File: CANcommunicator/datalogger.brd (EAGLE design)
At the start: 160 x 100 mm, 50 parts, among them IC1 0.1uF, IC2 1.0uF, IC3 0.1uF, IC4 0.1uF, IC5 LM2937, U1 TXB0104

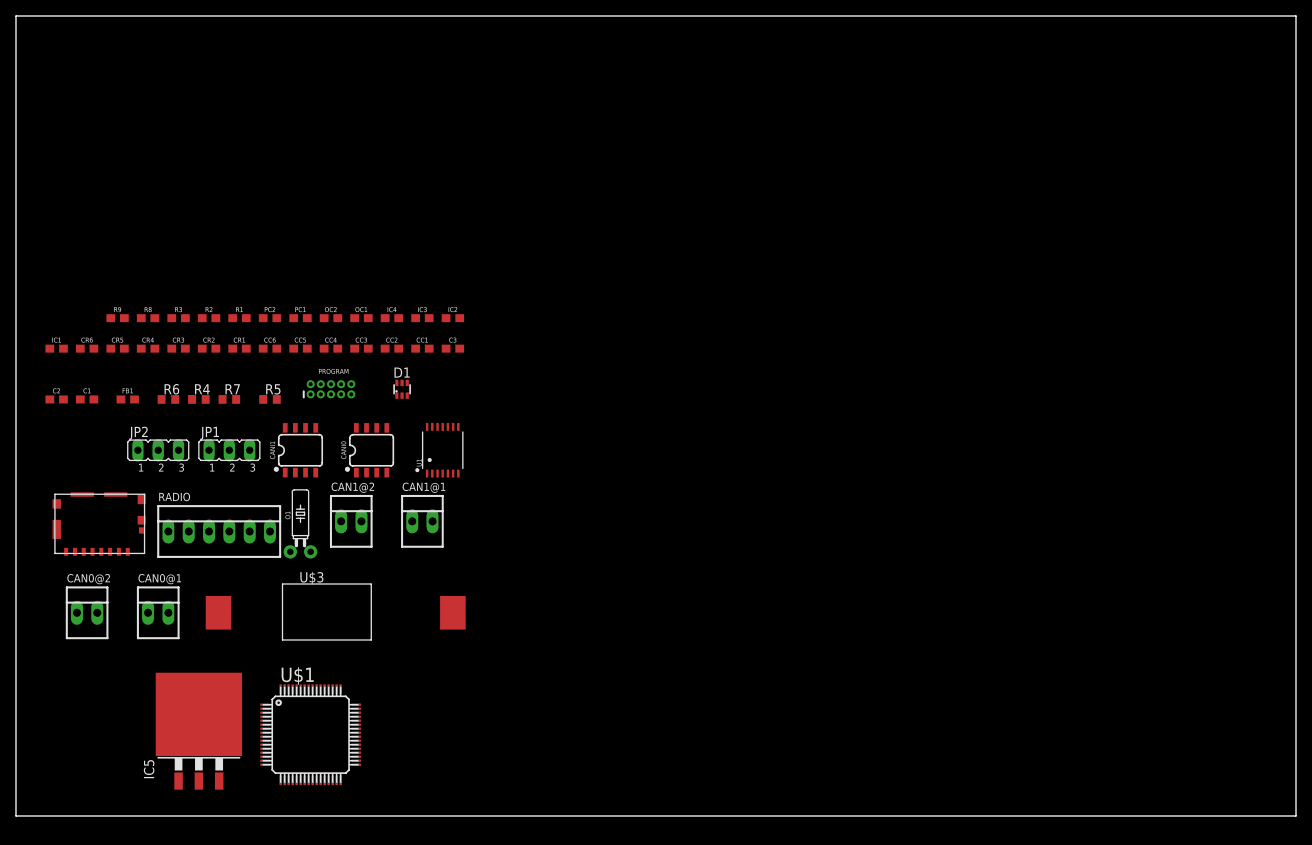
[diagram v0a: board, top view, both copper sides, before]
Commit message: First iteration of CAN datalogger using diode RTC
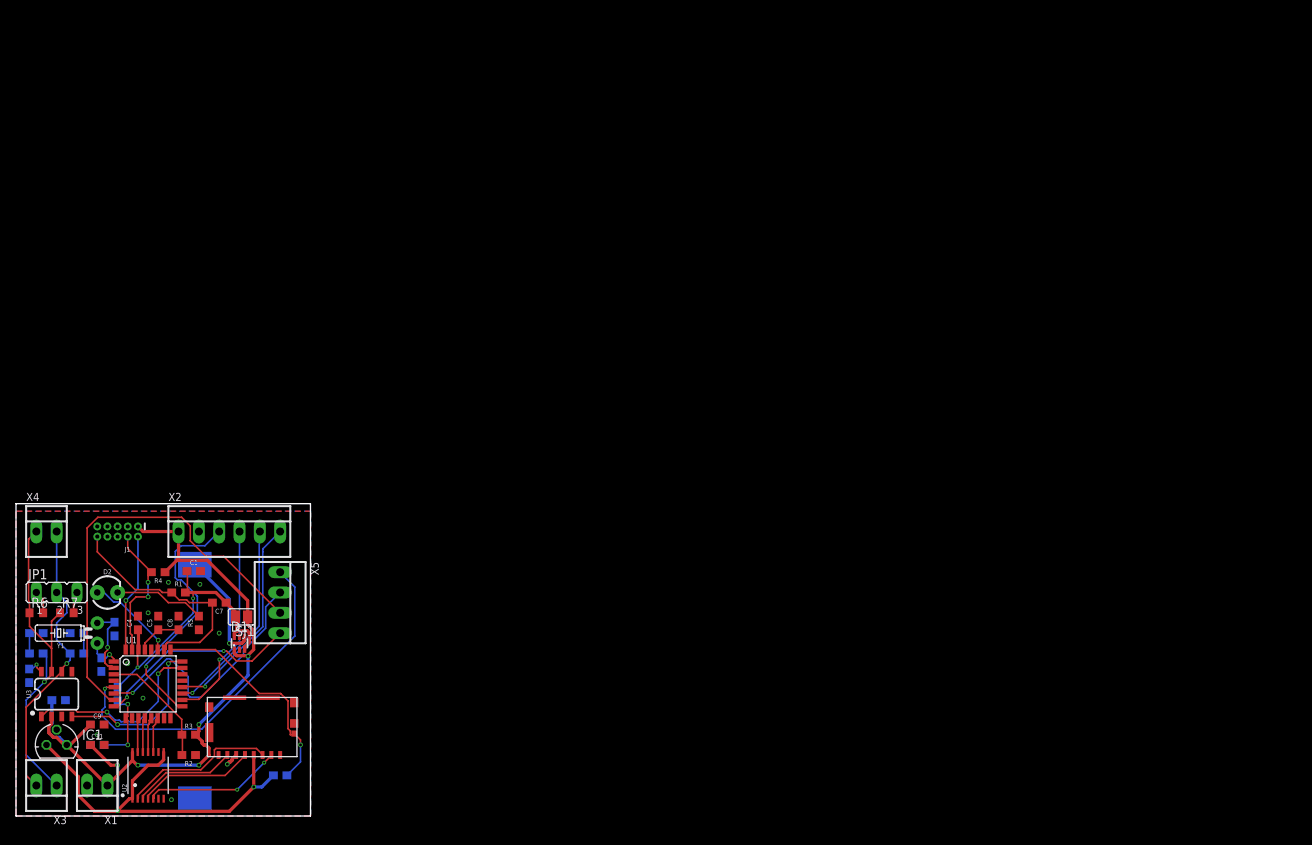
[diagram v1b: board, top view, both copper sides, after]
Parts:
- removed CAN0@1, CAN0@2, CAN1@1, CAN1@2: 22-23-2021, con-molex:22-23-2021
- removed CANI0, CANI1: MCP2551, SparkFun-IC-Comms:SO08
- removed CC1, CC6, IC3, IC4: 0.1uF, SparkFun-Capacitors:0603
- removed CC2, CC3, CC4, CC5: 560pF, SparkFun-Capacitors:0603
- removed CR1, CR4: 4.7k, SparkFun-Resistors:0603
- removed CR2, CR3, CR5, CR6: 100, SparkFun-Resistors:0603
- removed IC2: 1.0uF, SparkFun-Capacitors:0603
- removed IC5: LM2937, linear:TO263-3
- removed JP2: (no value), jumper:JP2
- removed O1: 32.768kHz, SparkFun-Clocks:CRYSTAL-PTH-2X6-CYL
- removed OC1, OC2: 12pF, SparkFun-Capacitors:0603
- removed PC1, PC2: 10uF, SparkFun-Capacitors:0603
- removed PROGRAM: CORTEX_DEBUG_PTH, SparkFun-Connectors:2X5-PTH-1.27MM
- removed RADIO: (no value), con-molex:22-23-2061
- removed U$1: ATSAMC21J18A-AU, washuracing:TQFP64-05
- removed U$2: WM14405CT-ND, washuracing:1051620001-SMD
- removed U$3: BU2032SM-FH-GCT-ND, washuracing:BU2032SM-FH-GCT-ND
- added BAT1: BU2032SM-FH-GCT-ND, washuracing:BAT_BU2032SM-BT-GTR
- added C10, C4, C8, C9: 0.1uF, SparkFun-Capacitors:0603
- added C11: 10uF, SparkFun-Capacitors:0603
- added C12, C13: 560pF, SparkFun-Capacitors:0603
- added C5: 1.0uF, SparkFun-Capacitors:0603
- added C6: 12pF, SparkFun-Capacitors:0603
- added C7: 100pF, SparkFun-Capacitors:0603
- added D2: GREEN, SparkFun-LED:LED_3MM
- added J1: CORTEX_DEBUG_PTH, SparkFun-Connectors:2X5-PTH-1.27MM
- added R10, R11: 100, SparkFun-Resistors:0603
- added SD1: WM14405CT-ND, washuracing:1051620001-SMD
- added SJ1: (no value), jumper:SJ
- added U2: TXB0104, SparkFun-IC-Comms:TSSOP14
- added U3: MCP2551, SparkFun-IC-Comms:SO08
- added X1, X3, X4: 22-23-2021, con-molex:22-23-2021
- added X2: (no value), con-molex:22-23-2061
- added X5: 22-23-2041, con-molex:22-23-2041
- added Y1: 32.768kHz, SparkFun-Clocks:CRYSTAL-PTH-2X6-CYL
- C1: value 100pF -> 10uF
- C2: value 0.1uF -> 10uF
- C3: value 10uF -> 12pF
- IC1: value 0.1uF -> (none); device SparkFun-Capacitors:0603 -> v-reg:78LXX
- R1: value 1k -> 2.2k
- R2: value 2.2k -> 100k
- R3: value 10k -> 100k
- R4: value 60 -> 1k; device rcl:R0603 -> SparkFun-Resistors:0603
- R5: value 120 -> 330; device rcl:R0603 -> SparkFun-Resistors:0603
- R8: value 100k -> 4.7k
- R9: value 100k -> 10k
- U1: value TXB0104 -> ATSAMC21E18A-AU; device SparkFun-IC-Comms:TSSOP14 -> washuracing:TQFP32-08
- moved R9 60.7 mm to (33.0, 5.08), flipped to the bottom
- moved C3 59.1 mm to (10.7, 18.9), flipped to the bottom, turned to 270 degrees
- moved R2 54.7 mm to (21.6, 7.62), turned to 180 degrees
- moved R3 52.1 mm to (21.6, 10.2)
- moved IC1 49.5 mm to (5.08, 8.89)
- moved R8 47.1 mm to (1.65, 17.5), flipped to the bottom, turned to 270 degrees
- moved U1 47.0 mm to (16.5, 16.5)
- moved C2 43.5 mm to (10.2, 8.89), flipped to the bottom
- moved D1 37.7 mm to (27.9, 21.6)
- moved FB1 36.9 mm to (12.7, 15.2), flipped to the bottom, turned to 270 degrees
- moved R1 35.1 mm to (20.3, 27.9)
- moved R7 33.5 mm to (6.35, 25.4)
- moved R6 31.4 mm to (2.54, 25.4)
- moved R5 29.3 mm to (22.9, 24.1), turned to 90 degrees
- moved JP1 28.0 mm to (5.08, 27.9)
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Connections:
- removed net C1HRC1: CC4.1, CR6.1
- removed net C1LRC1: CC5.1, CR5.1
- removed net C1RS1: CANI1.8, CR4.1
- removed net CAN1H: CAN1@1.1, CAN1@2.1, CANI1.7, CR6.2, R6.1, R7.1
- removed net CAN1L: CAN1@1.2, CAN1@2.2, CANI1.6, CR5.2, JP2.2
- removed net CAN1RX: CANI1.4, U$1.24
- removed net CAN1TX: CANI1.1, U$1.23
- removed net N$1: RADIO.3, U$1.17
- removed net N$2: RADIO.4, U$1.18
- removed net N$3: RADIO.5, U$1.19
- removed net N$4: RADIO.6, U$1.20
- removed net N$6: JP2.1, R6.2
- removed net N$8: JP2.3, R7.2
- removed net N$9: D1.4, U$3.VBAT
- removed net UCVCC: D1.3, D1.6
- removed net VDDANA: FB1.2, PC2.1, U$1.8
- new net CONN0: U1.5, X5.1
- new net CONN1: U1.6, X5.2
- new net CONN2: U1.7, X5.3
- new net CONN3: U1.8, X5.4
- new net LEDA: D2.A, U1.27
- new net LEDC: D2.K, R5.2
- new net RADIO0: U1.17, X2.3
- new net RADIO1: U1.18, X2.4
- new net RADIO2: U1.19, X2.5
- new net RADIO3: U1.20, X2.6
- new net VBAT: BAT1.1, D1.4
- new net VCC_2: C1.1, C4.1, C7.1, D1.3, D1.6, FB1.1, R1.2, SJ1.2, U1.30
- new net VDDANA1: C2.1, FB1.2, U1.9
- net 3.3V: now also C11.1, IC1.OUT, R9.2, SD1.PIN4, U2.1, U2.8; no longer C3.1, IC5.3, R3.2, U$2.PIN4, U1.1, U1.8
- net 3VCS: now also SD1.PIN2, U2.5; no longer U$2.PIN2, U1.5
- net 3VSCK: now also SD1.PIN5, U2.4; no longer U$2.PIN5, U1.4
- net 3VSI: now also SD1.PIN3, U2.2; no longer U$2.PIN3, U1.2
- net 3VSO: now also SD1.PIN7, U2.3; no longer U$2.PIN7, U1.3
- net C1HRC: now also C12.1, R10.1; no longer CC2.1, CR2.1
- net C1LRC: now also C13.1, R11.1; no longer CC3.1, CR3.1
- net C1RS: now also R8.1, U3.8; no longer CANI0.8, CR1.1
- net CAN0H: now also R10.2, R6.1, R7.1, U3.7, X3.1, X4.1; no longer CAN0@1.1, CAN0@2.1, CANI0.7, CR2.2, R4.1, R5.1
- net CAN0L: now also R11.2, U3.6, X3.2, X4.2; no longer CAN0@1.2, CAN0@2.2, CANI0.6, CR3.2
- net CAN0RX: now also U1.24, U3.4; no longer CANI0.4, U$1.46
- net CAN0TX: now also U1.23, U3.1; no longer CANI0.1, U$1.45
- net GND: now also BAT1.2, C1.2, C10.1, C11.2, C12.2, C13.2, C4.2, C5.2, C6.2, C8.2, C9.2, IC1.GND, J1.3, J1.5, J1.9, R2.1, R5.1, R8.2, SD1.G1, SD1.G2, SD1.G3, SD1.G4, SD1.PIN6, U1.10, U1.28, U2.7, U3.3, X1.2, X2.2; no longer CANI0.3, CANI1.3, CC1.1, CC2.2, CC3.2, CC4.2, CC5.2, CC6.1, CR1.2, CR4.2, IC1.2, IC2.2, IC3.2, IC4.2, IC5.2, OC1.1, OC2.1, PC1.2, PC2.2, PROGRAM.3, PROGRAM.5, PROGRAM.9, R9.1, RADIO.2, U$1.22, U$1.33, U$1.47, U$1.54, U$1.7, U$2.G1, U$2.G2, U$2.G3, U$2.G4, U$2.PIN6, U$3.GND, U1.7
- net N$5: now also R6.2; no longer R4.2
- net N$7: now also R7.2; no longer R5.2
- net PWRLOSS: now also R2.2, R3.1, U1.3; no longer R8.1, R9.2
- net RESET_L: now also C7.2, J1.10, R1.1, U1.26; no longer C1.2, PROGRAM.10, R2.1, U$1.52
- net SDCS: now also U1.14, U2.10; no longer U$1.42, U1.10
- net SDMISO: now also U2.12; no longer U$1.40
- net SDMOSI: now also U1.11, U2.13; no longer U$1.39, U1.13
- net SDSCK: now also U1.13, U2.11; no longer U$1.41, U1.11
- net SD_CD: now also R9.1, SD1.PIN9, U1.25; no longer R3.1, U$1.49, U$2.PIN9
- net SWDCLK: now also J1.4, R4.2, U1.31; no longer PROGRAM.4, R1.2, U$1.57
- net SWDIO: now also J1.2, U1.32; no longer PROGRAM.2, U$1.58
- net VCC: now also C10.2, C9.1, IC1.IN, J1.1, R3.2, R4.1, SJ1.1, U2.14, U3.2, X1.1, X2.1; no longer C1.1, C2.1, CANI0.2, CANI1.2, CC1.2, CC6.2, FB1.1, IC1.1, IC4.1, IC5.1, PC1.1, PROGRAM.1, R1.1, R2.2, R8.2, RADIO.1, U$1.21, U$1.34, U$1.48, U$1.56, U1.14
- net VDDCORE: now also C5.1, C8.1, U1.29; no longer IC2.1, IC3.1, U$1.55
- net XIN32: now also C3.1, U1.1, Y1.1; no longer O1.2, OC2.2, U$1.1
- net XOUT32: now also C6.1, U1.2, Y1.2; no longer O1.1, OC1.2, U$1.2
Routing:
- net VCC: track 0.00 -> 87.0 mm, vias 0 -> 4
- net 3.3V: track 0.00 -> 59.9 mm, vias 0 -> 3
- net CONN2: track 0.00 -> 53.9 mm
- net CAN0H: track 0.00 -> 44.9 mm, vias 0 -> 1
- net CONN0: track 0.00 -> 43.1 mm, vias 0 -> 1
- net VCC_2: track 0.00 -> 38.1 mm, vias 0 -> 2
- net CAN0L: track 0.00 -> 36.3 mm, vias 0 -> 1
- net CONN1: track 0.00 -> 33.2 mm, vias 0 -> 1
- net RADIO0: track 0.00 -> 32.2 mm, vias 0 -> 1
- net RESET_L: track 0.00 -> 29.8 mm
- net SD_CD: track 0.00 -> 28.5 mm, vias 0 -> 1
- net RADIO3: track 0.00 -> 26.2 mm, vias 0 -> 1
- net CONN3: track 0.00 -> 26.0 mm, vias 0 -> 2
- net RADIO1: track 0.00 -> 25.4 mm, vias 0 -> 1
- net RADIO2: track 0.00 -> 25.0 mm, vias 0 -> 1
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- added copper zone on layer 1, net GND
- added copper zone on layer 16, net GND
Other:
- board size 160 x 100 mm -> 36.8 x 39 mm

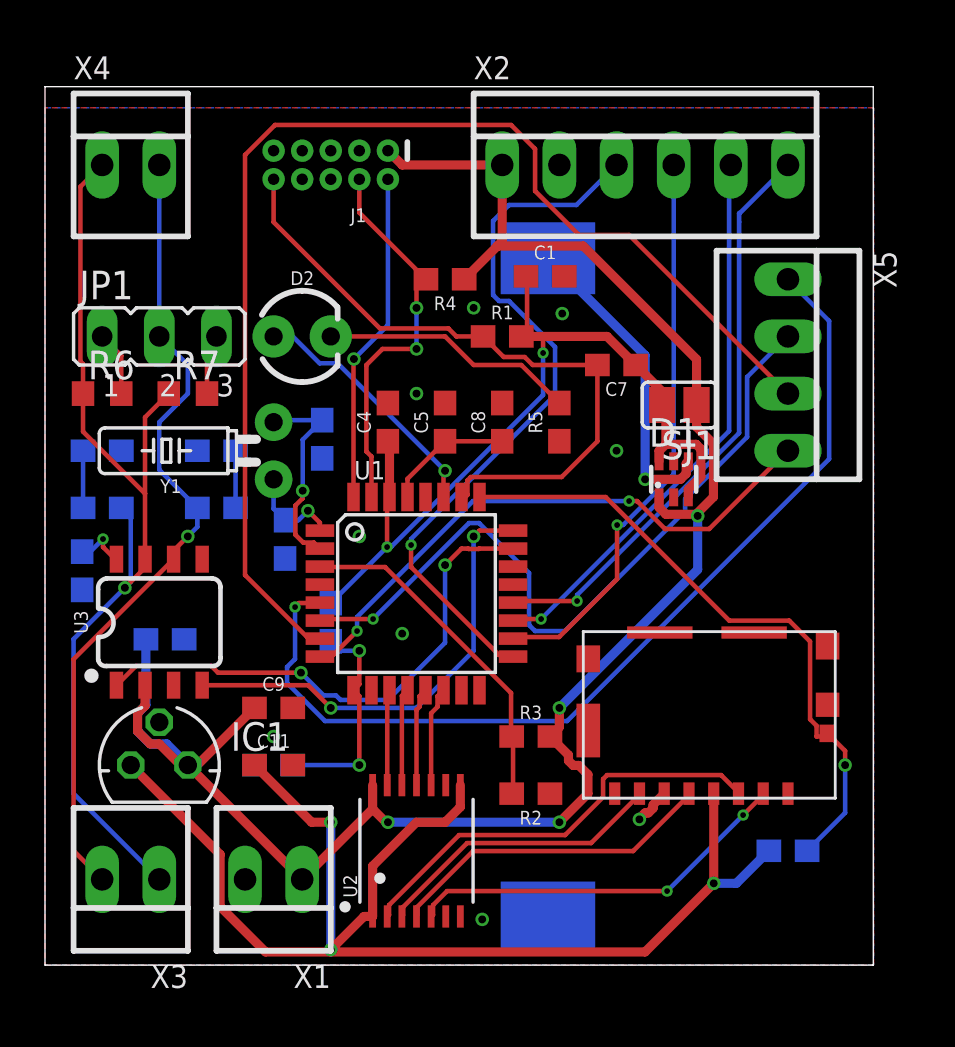
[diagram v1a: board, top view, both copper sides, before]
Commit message: Diode-less battery RTC with external IC
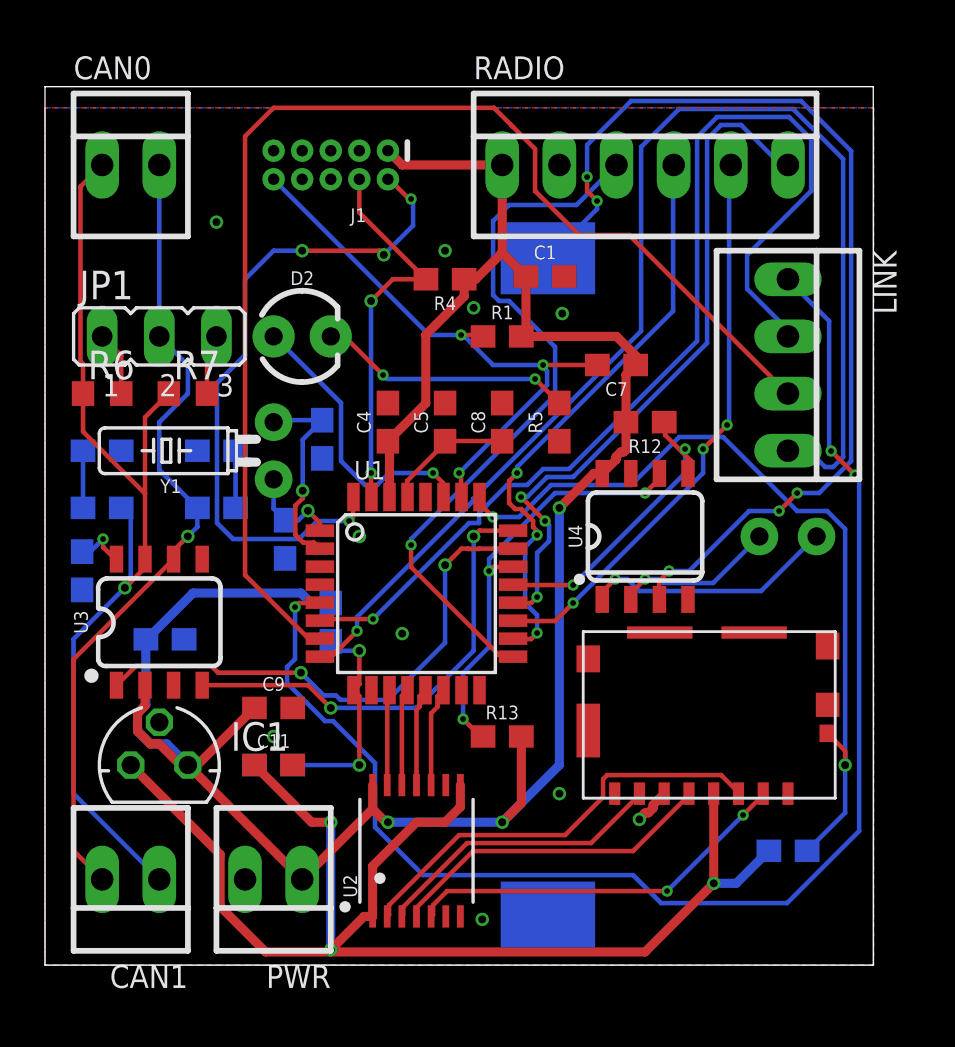
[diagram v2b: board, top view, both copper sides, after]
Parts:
- removed D1: BAS70-07S, diode:SOT363_PHILIPS
- removed R2, R3: 100k, SparkFun-Resistors:0603
- removed SJ1: (no value), jumper:SJ
- added R12, R13: 680, SparkFun-Resistors:0603
- added U4: DS1307Z, SparkFun-Clocks:SO08-0.15
- added Y2: 32.768kHz, SparkFun-Clocks:CRYSTAL-PTH-2X6-CYL
- renumbered X1 to PWR, X2 to RADIO, X3 to CAN1, X4 to CAN0, X5 to LINK
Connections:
- removed net PWRLOSS: R2.2, R3.1, U1.3
- removed net VBAT: BAT1.1, D1.4
- removed net VCC_2: C1.1, C4.1, C7.1, D1.3, D1.6, FB1.1, R1.2, SJ1.2, U1.30
- new net N$1: BAT1.1, U4.3
- new net N$4: U4.1, Y2.2
- new net N$6: U4.2, Y2.1
- new net RTCSCL: R13.1, U1.22, U4.6
- new net RTCSDA: R12.1, U1.21, U4.5
- net GND: now also U4.4; no longer R2.1
- net VCC: now also C1.1, C4.1, C7.1, FB1.1, R1.2, R12.2, R13.2, U1.30, U4.8; no longer D1.1, R3.2, SJ1.1
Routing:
- net N$1: track 0.00 -> 44.9 mm, vias 0 -> 5
- net VCC_2: track 38.1 -> 0.00 mm, vias 2 -> 0
- net CONN3: track 26.0 -> 55.7 mm, vias 2 -> 1
- net CONN0: track 43.1 -> 63.1 mm, vias 1 -> 3
- net RTCSCL: track 0.00 -> 19.3 mm, vias 0 -> 3
- net VCC: track 87.0 -> 103.9 mm, vias 4 -> 3
- net SWDIO: track 14.8 -> 30.4 mm, vias 1 -> 4
- net PWRLOSS: track 15.4 -> 0.00 mm
- net CONN1: track 33.2 -> 47.8 mm
- net VBAT: track 14.1 -> 0.00 mm, vias 1 -> 0
- net RTCSDA: track 0.00 -> 13.8 mm, vias 0 -> 2
- net N$4: track 0.00 -> 11.3 mm, vias 0 -> 1
- net SD_CD: track 28.5 -> 36.7 mm, vias 1 -> 2
- net N$6: track 0.00 -> 7.19 mm, vias 0 -> 1
- net RADIO3: track 26.2 -> 31.2 mm, vias 1 -> 3
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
